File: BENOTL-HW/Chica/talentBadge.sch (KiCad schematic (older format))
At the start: 56 parts, among them P1 USB_A, P2 OLED, P3 Batt, P4 PS, Q1 MMBT3904, Q2 MMBT3904, Q3 IR phototransistor, SW1 B1, SW2 B2, SW3 RST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

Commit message: Agregado KeyStone_2479
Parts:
- P3: footprint Pin_Headers:Pin_Header_Straight_1x02_Pitch2.54mm -> talentBadge:Keystone_2479_3xAAA
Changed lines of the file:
@@
 LIBS:contrib
 LIBS:valves
-LIBS:pdxlbs
+LIBS:ESP8266
 LIBS:pspice
 LIBS:Video
-LIBS:Valve
 LIBS:Triac_Thyristor
-LIBS:Transistor_IGBT
-LIBS:Transistor_FET
-LIBS:Transistor_BJT
-LIBS:Transistor_Array
-LIBS:Transformer
-LIBS:Timer_RTC
-LIBS:Timer_PLL
-LIBS:Timer
-LIBS:Switch
-LIBS:Sensor_Voltage
-LIBS:Sensor_Touch
-LIBS:Sensor_Temperature
-LIBS:Sensor_Proximity
-LIBS:Sensor_Pressure
-LIBS:Sensor_Optical
-LIBS:Sensor_Motion
-LIBS:Sensor_Magnetic
-LIBS:Sensor_Humidity
-LIBS:Sensor_Gas
-LIBS:Sensor_Current
-LIBS:Sensor_Audio
-LIBS:Sensor
-LIBS:Relay_SolidState
-LIBS:Relay
-LIBS:Regulator_Switching
-LIBS:Regulator_SwitchedCapacitor
-LIBS:Regulator_Linear
-LIBS:Regulator_Current
-LIBS:Regulator_Controller
-LIBS:Reference_Voltage
-LIBS:Reference_Current
-LIBS:RF_ZigBee
-LIBS:RF_WiFi
-LIBS:RF_Switch
-LIBS:RF_RFID
-LIBS:RF_Module
-LIBS:RF_Mixer
-LIBS:RF_GPS
-LIBS:RF_Bluetooth
-LIBS:RF_AM_FM
-LIBS:RF
-LIBS:Power_Supervisor
-LIBS:Power_Protection
 LIBS:Power_Management
-LIBS:Potentiometer_Digital
-LIBS:Oscillator
-LIBS:Motor
-LIBS:Memory_UniqueID
-LIBS:Memory_ROM
-LIBS:Memory_RAM
-LIBS:Memory_NVRAM
-LIBS:Memory_Flash
-LIBS:Memory_EPROM
-LIBS:Memory_EEPROM
-LIBS:Memory_Controller
 LIBS:Mechanical
-LIBS:MCU_Texas_MSP430
-LIBS:MCU_Texas
-LIBS:MCU_SiliconLabs
-LIBS:MCU_SiFive
-LIBS:MCU_ST_STM8
-LIBS:MCU_ST_STM32
-LIBS:MCU_Parallax
-LIBS:MCU_NXP_S08
-LIBS:MCU_NXP_MCore
-LIBS:MCU_NXP_MAC7100
-LIBS:MCU_NXP_LPC
-LIBS:MCU_NXP_Kinetis
-LIBS:MCU_NXP_HCS12
-LIBS:MCU_NXP_HC12
-LIBS:MCU_NXP_HC11
-LIBS:MCU_NXP_ColdFire
-LIBS:MCU_Module
-LIBS:MCU_Microchip_SAML
-LIBS:MCU_Microchip_SAME
-LIBS:MCU_Microchip_PIC32
-LIBS:MCU_Microchip_PIC24
-LIBS:MCU_Microchip_PIC18
-LIBS:MCU_Microchip_PIC16
-LIBS:MCU_Microchip_PIC12
-LIBS:MCU_Microchip_PIC10
-LIBS:MCU_Intel
-LIBS:MCU_Infineon
-LIBS:MCU_Cypress
-LIBS:MCU_Atmel_AVR
-LIBS:MCU_Atmel_ATTINY
-LIBS:MCU_Atmel_ATMEGA
-LIBS:MCU_Atmel_8051
-LIBS:MCU_AnalogDevices
-LIBS:Logic_TTL_IEEE
 LIBS:Logic_Programmable
-LIBS:Logic_LevelTranslator
-LIBS:Logic_CMOS_IEEE
-LIBS:Logic_CMOS_4000
-LIBS:Logic_74xx
-LIBS:Logic_74xgxx
-LIBS:LED
-LIBS:Jumper
-LIBS:Isolator_Analog
-LIBS:Isolator
-LIBS:Interface_USB
-LIBS:Interface_UART
-LIBS:Interface_Telecom
-LIBS:Interface_Optical
-LIBS:Interface_LineDriver
-LIBS:Interface_HID
-LIBS:Interface_Expansion
-LIBS:Interface_Ethernet
-LIBS:Interface_CurrentLoop
-LIBS:Interface_CAN_LIN
 LIBS:Interface
 LIBS:Graphic
-LIBS:GPU
-LIBS:Filter
-LIBS:FPGA_Xilinx_Virtex7
-LIBS:FPGA_Xilinx_Virtex6
-LIBS:FPGA_Xilinx_Virtex5
-LIBS:FPGA_Xilinx_Spartan6
-LIBS:FPGA_Xilinx_Kintex7
-LIBS:FPGA_Xilinx_Artix7
-LIBS:FPGA_Xilinx
-LIBS:FPGA_Actel
-LIBS:Driver_Relay
-LIBS:Driver_Motor
-LIBS:Driver_LED
-LIBS:Driver_FET
-LIBS:Driver_Display
-LIBS:Display_Graphic
-LIBS:Display_Character
-LIBS:Diode_Laser
-LIBS:Diode_Bridge
 LIBS:Diode
 LIBS:Device
-LIBS:DSP_Texas
-LIBS:DSP_Motorola
-LIBS:DSP_Microchip_DSPIC33
-LIBS:DSP_Freescale
-LIBS:Converter_DCDC
-LIBS:Converter_ACDC
-LIBS:Connector_Specialized
-LIBS:Connector_Generic_Shielded
-LIBS:Connector_Generic
-LIBS:Comparator
-LIBS:CPU_PowerPC
-LIBS:CPU_NXP_68000
-LIBS:CPU_NXP_6800
-LIBS:CPU
-LIBS:CPLD_Xilinx
-LIBS:CPLD_Altera
 LIBS:Battery_Management
 LIBS:Audio
-LIBS:Analog_Switch
-LIBS:Analog_DAC
-LIBS:Analog_ADC
-LIBS:Analog
-LIBS:Amplifier_Video
-LIBS:Amplifier_Operational
-LIBS:Amplifier_Instrumentation
-LIBS:Amplifier_Difference
-LIBS:Amplifier_Current
-LIBS:Amplifier_Buffer
-LIBS:Amplifier_Audio
 LIBS:talentBadge-cache
 EELAYER 25 0
@@
 B2
 $Comp
-L +3.3V #PWR014
+L +3.3V #PWR011
 U 1 1 5A8ACE92
 P 8750 4150
-F 0 "#PWR014" H 8750 4000 50  0001 C CNN
+F 0 "#PWR011" H 8750 4000 50  0001 C CNN
 F 1 "+3.3V" H 8750 4290 50  0000 C CNN
 F 2 "" H 8750 4150 50  0000 C CNN
@@
 $EndComp
 $Comp
-L GND #PWR015
+L GND #PWR012
 U 1 1 5A8B6B0C
 P 8600 4600
-F 0 "#PWR015" H 8600 4350 50  0001 C CNN
+F 0 "#PWR012" H 8600 4350 50  0001 C CNN
 F 1 "GND" H 8450 4550 50  0000 C CNN
 F 2 "" H 8600 4600 50  0000 C CNN
@@
 $EndComp
 $Comp
-L GND #PWR016
+L GND #PWR013
 U 1 1 5A8BA4F2
 P 9050 6200
-F 0 "#PWR016" H 9050 5950 50  0001 C CNN
+F 0 "#PWR013" H 9050 5950 50  0001 C CNN
 F 1 "GND" H 9050 6050 50  0000 C CNN
 F 2 "" H 9050 6200 50  0000 C CNN
@@
 $EndComp
 $Comp
-L +3.3V #PWR017
+L +3.3V #PWR014
 U 1 1 5A8CF103
 P 3700 6000
-F 0 "#PWR017" H 3700 5850 50  0001 C CNN
+F 0 "#PWR014" H 3700 5850 50  0001 C CNN
 F 1 "+3.3V" H 3700 6140 50  0000 C CNN
 F 2 "" H 3700 6000 50  0000 C CNN
@@
 $EndComp
 $Comp
-L +3.3V #PWR018
+L +3.3V #PWR015
 U 1 1 5A8CF265
 P 4535 4300
-F 0 "#PWR018" H 4535 4150 50  0001 C CNN
+F 0 "#PWR015" H 4535 4150 50  0001 C CNN
 F 1 "+3.3V" H 4535 4440 50  0000 C CNN
 F 2 "" H 4535 4300 50  0000 C CNN
@@
 $EndComp
 $Comp
-L GND #PWR019
+L GND #PWR016
 U 1 1 5A8CFC33
 P 4650 4900
-F 0 "#PWR019" H 4650 4650 50  0001 C CNN
+F 0 "#PWR016" H 4650 4650 50  0001 C CNN
 F 1 "GND" H 4650 4750 50  0000 C CNN
 F 2 "" H 4650 4900 50  0000 C CNN
@@
 F 0 "P3" H 650 6500 50  0000 C CNN
 F 1 "Batt" V 750 6350 50  0000 C CNN
-F 2 "Pin_Headers:Pin_Header_Straight_1x02_Pitch2.54mm" H 650 6350 50  0001 C CNN
+F 2 "talentBadge:Keystone_2479_3xAAA" H 650 6350 50  0001 C CNN
 F 3 "" H 650 6350 50  0000 C CNN
 	1    650  6350
@@
 IRL
 $Comp
-L GND #PWR020
+L GND #PWR017
 U 1 1 5A914774
 P 6200 5150
-F 0 "#PWR020" H 6200 4900 50  0001 C CNN
+F 0 "#PWR017" H 6200 4900 50  0001 C CNN
 F 1 "GND" H 6200 5000 50  0000 C CNN
 F 2 "" H 6200 5150 50  0000 C CNN
@@
 $EndComp
 $Comp
-L +3.3V #PWR021
+L +3.3V #PWR018
 U 1 1 5A916FB2
 P 6200 3850
-F 0 "#PWR021" H 6200 3700 50  0001 C CNN
+F 0 "#PWR018" H 6200 3700 50  0001 C CNN
 F 1 "+3.3V" H 6200 3990 50  0000 C CNN
 F 2 "" H 6200 3850 50  0000 C CNN
@@
 $EndComp
 $Comp
-L +3.3V #PWR022
+L +3.3V #PWR019
 U 1 1 5A8CED38
 P 7775 1585
-F 0 "#PWR022" H 7775 1435 50  0001 C CNN
+F 0 "#PWR019" H 7775 1435 50  0001 C CNN
 F 1 "+3.3V" H 7775 1725 50  0000 C CNN
 F 2 "" H 7775 1585 50  0000 C CNN
@@
 NoConn ~ 10550 4800
 $Comp
-L GND #PWR023
+L GND #PWR020
 U 1 1 5A9146B5
 P 5700 5150
-F 0 "#PWR023" H 5700 4900 50  0001 C CNN
+F 0 "#PWR020" H 5700 4900 50  0001 C CNN
 F 1 "GND" H 5700 5000 50  0000 C CNN
 F 2 "" H 5700 5150 50  0000 C CNN
@@
 Connection ~ 8030 1475
 $Comp
-L +3.3V #PWR024
+L +3.3V #PWR021
 U 1 1 5AA16781
 P 8025 1415
-F 0 "#PWR024" H 8025 1265 50  0001 C CNN
+F 0 "#PWR021" H 8025 1265 50  0001 C CNN
 F 1 "+3.3V" H 8025 1555 50  0000 C CNN
 F 2 "" H 8025 1415 50  0000 C CNN
@@
 $EndComp
 $Comp
-L GND #PWR025
+L GND #PWR022
 U 1 1 5AA16E5F
 P 10830 2575
-F 0 "#PWR025" H 10830 2325 50  0001 C CNN
+F 0 "#PWR022" H 10830 2325 50  0001 C CNN
 F 1 "GND" H 10830 2425 50  0000 C CNN
 F 2 "" H 10830 2575 50  0000 C CNN
@@
 	9315 2940 9315 3060
 $Comp
-L GND #PWR026
+L GND #PWR023
 U 1 1 5AA1CD61
 P 9315 3060
-F 0 "#PWR026" H 9315 2810 50  0001 C CNN
+F 0 "#PWR023" H 9315 2810 50  0001 C CNN
 F 1 "GND" H 9315 2910 50  0000 C CNN
 F 2 "" H 9315 3060 50  0000 C CNN

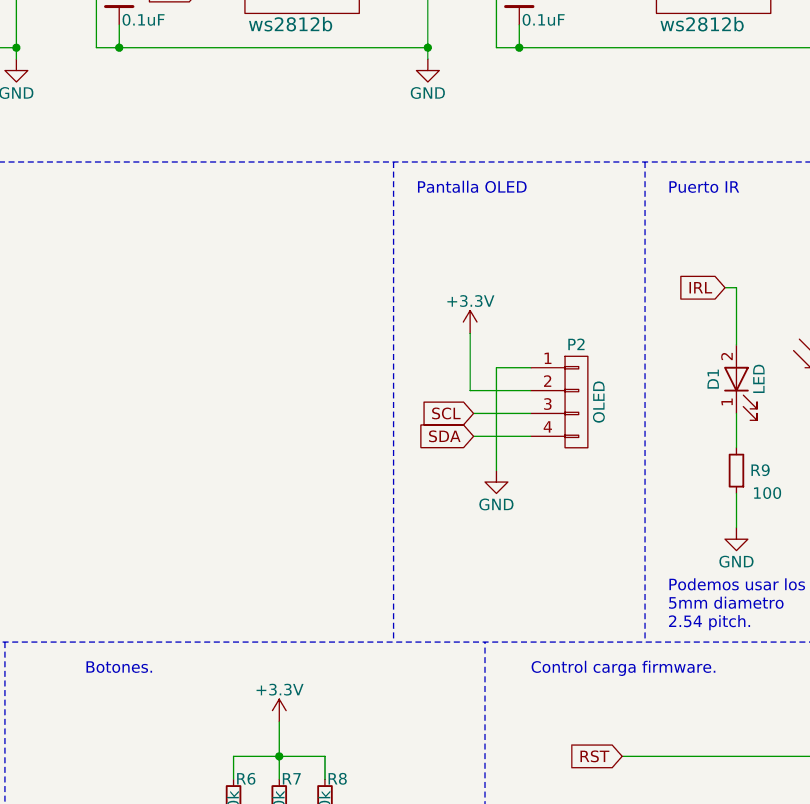
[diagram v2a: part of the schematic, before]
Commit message: Chica - I2C pullupt
Se agregan pullups a linea i2c para display.
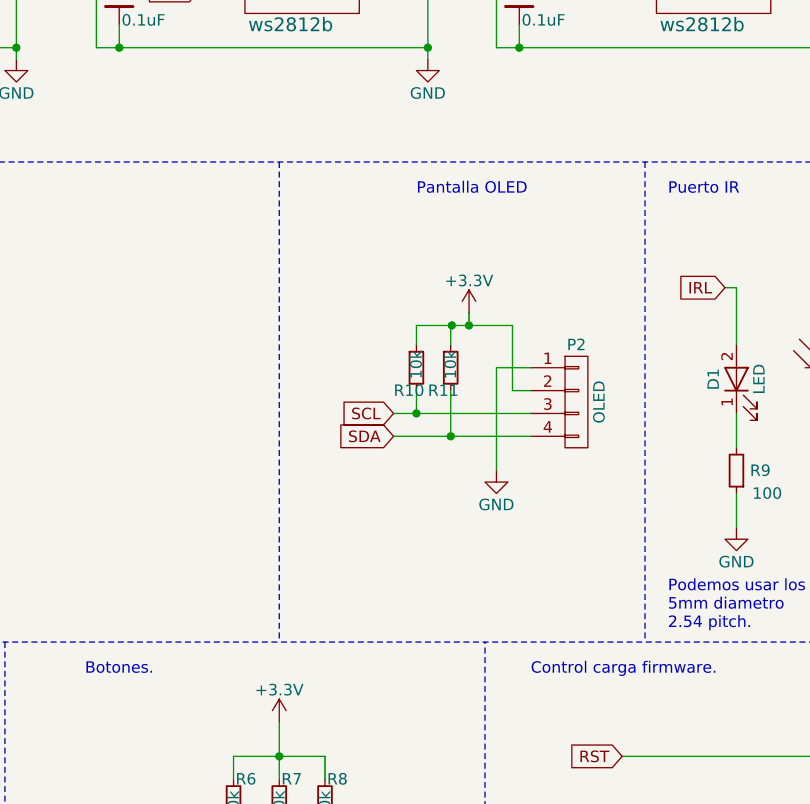
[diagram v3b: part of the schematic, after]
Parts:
- added R10, R11: 10k, Resistors_SMD:R_0805_HandSoldering, symbol R_Small
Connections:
- net +3V3: now also R10.1, R11.1
- net SCL: now also R10.2
- net SDA: now also R11.2
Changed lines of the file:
@@
 L +3.3V #PWR015
 U 1 1 5A8CF265
-P 4535 4300
-F 0 "#PWR015" H 4535 4150 50  0001 C CNN
-F 1 "+3.3V" H 4535 4440 50  0000 C CNN
-F 2 "" H 4535 4300 50  0000 C CNN
-F 3 "" H 4535 4300 50  0000 C CNN
-	1    4535 4300
+P 4530 4210
+F 0 "#PWR015" H 4530 4060 50  0001 C CNN
+F 1 "+3.3V" H 4530 4350 50  0000 C CNN
+F 2 "" H 4530 4210 50  0000 C CNN
+F 3 "" H 4530 4210 50  0000 C CNN
+	1    4530 4210
 	1    0    0    -1
 $EndComp
@@
 	1    0    0    -1
 $EndComp
-Text GLabel 4550 4750 0    50   Input ~ 0
+Text GLabel 4200 4750 0    50   Input ~ 0
 SDA
-Text GLabel 4550 4650 0    50   Input ~ 0
+Text GLabel 4200 4650 0    50   Input ~ 0
 SCL
 Text GLabel 8090 2140 0    50   Output ~ 0
@@
 	1    0    0    -1
 $EndComp
+$Comp
+L +3.3V #PWR021
+U 1 1 5AA16781
+P 8025 1415
+F 0 "#PWR021" H 8025 1265 50  0001 C CNN
+F 1 "+3.3V" H 8025 1555 50  0000 C CNN
+F 2 "" H 8025 1415 50  0000 C CNN
+F 3 "" H 8025 1415 50  0000 C CNN
+	1    8025 1415
+	1    0    0    -1
+$EndComp
+$Comp
+L GND #PWR022
+U 1 1 5AA16E5F
+P 10830 2575
+F 0 "#PWR022" H 10830 2325 50  0001 C CNN
+F 1 "GND" H 10830 2425 50  0000 C CNN
+F 2 "" H 10830 2575 50  0000 C CNN
+F 3 "" H 10830 2575 50  0000 C CNN
+	1    10830 2575
+	1    0    0    -1
+$EndComp
+NoConn ~ 10485 1940
+$Comp
+L GND #PWR023
+U 1 1 5AA1CD61
+P 9315 3060
+F 0 "#PWR023" H 9315 2810 50  0001 C CNN
+F 1 "GND" H 9315 2910 50  0000 C CNN
+F 2 "" H 9315 3060 50  0000 C CNN
+F 3 "" H 9315 3060 50  0000 C CNN
+	1    9315 3060
+	1    0    0    -1
+$EndComp
+$Comp
+L R_Small R10
+U 1 1 5AA6BBDB
+P 4300 4450
+F 0 "R10" H 4200 4350 50  0000 L CNN
+F 1 "10k" V 4300 4400 50  0000 L CNN
+F 2 "Resistors_SMD:R_0805_HandSoldering" H 4300 4450 50  0001 C CNN
+F 3 "https://www.mouser.com/ds/2/447/Yageo_08112016_RC0805-1211991.pdf" H 4300 4450 50  0001 C CNN
+F 4 "RC0805FR-0710KL" H 4300 4450 60  0001 C CNN "PartNo"
+	1    4300 4450
+	1    0    0    -1
+$EndComp
+$Comp
+L R_Small R11
+U 1 1 5AA6BCEE
+P 4450 4450
+F 0 "R11" H 4350 4350 50  0000 L CNN
+F 1 "10k" V 4450 4400 50  0000 L CNN
+F 2 "Resistors_SMD:R_0805_HandSoldering" H 4450 4450 50  0001 C CNN
+F 3 "https://www.mouser.com/ds/2/447/Yageo_08112016_RC0805-1211991.pdf" H 4450 4450 50  0001 C CNN
+F 4 "RC0805FR-0710KL" H 4450 4450 60  0001 C CNN "PartNo"
+	1    4450 4450
+	1    0    0    -1
+$EndComp
 Wire Wire Line
 	3000 6550 2900 6550
@@
 Connection ~ 3900 6850
 Wire Wire Line
-	4535 4300 4535 4550
-Wire Wire Line
 	4650 4450 4650 4900
 Wire Wire Line
-	4550 4650 4800 4650
-Wire Wire Line
-	4800 4750 4550 4750
+	4200 4650 4800 4650
+Wire Wire Line
+	4200 4750 4800 4750
 Wire Wire Line
 	8100 2440 8100 2640
@@
 	6900 5650 6900 5600
 Wire Notes Line
-	4200 3550 4200 5650
+	3700 3550 3700 5650
 Wire Wire Line
 	8100 4800 9350 4800
@@
 	4650 4450 4800 4450
 Wire Wire Line
-	4535 4550 4800 4550
-Wire Wire Line
 	8315 1740 8075 1740
 Wire Wire Line
@@
 	8030 1415 8025 1415
 Connection ~ 8030 1475
-$Comp
-L +3.3V #PWR021
-U 1 1 5AA16781
-P 8025 1415
-F 0 "#PWR021" H 8025 1265 50  0001 C CNN
-F 1 "+3.3V" H 8025 1555 50  0000 C CNN
-F 2 "" H 8025 1415 50  0000 C CNN
-F 3 "" H 8025 1415 50  0000 C CNN
-	1    8025 1415
-	1    0    0    -1
-$EndComp
-$Comp
-L GND #PWR022
-U 1 1 5AA16E5F
-P 10830 2575
-F 0 "#PWR022" H 10830 2325 50  0001 C CNN
-F 1 "GND" H 10830 2425 50  0000 C CNN
-F 2 "" H 10830 2575 50  0000 C CNN
-F 3 "" H 10830 2575 50  0000 C CNN
-	1    10830 2575
-	1    0    0    -1
-$EndComp
 Wire Wire Line
 	10830 1740 10830 2575
 Connection ~ 10830 2240
-NoConn ~ 10485 1940
 Wire Wire Line
 	8315 2440 8000 2440
@@
 Wire Wire Line
 	9315 2940 9315 3060
-$Comp
-L GND #PWR023
-U 1 1 5AA1CD61
-P 9315 3060
-F 0 "#PWR023" H 9315 2810 50  0001 C CNN
-F 1 "GND" H 9315 2910 50  0000 C CNN
-F 2 "" H 9315 3060 50  0000 C CNN
-F 3 "" H 9315 3060 50  0000 C CNN
-	1    9315 3060
-	1    0    0    -1
-$EndComp
+Wire Wire Line
+	4300 4350 4300 4265
+Wire Wire Line
+	4300 4265 4720 4265
+Wire Wire Line
+	4530 4265 4530 4210
+Wire Wire Line
+	4450 4350 4450 4265
+Wire Wire Line
+	4450 4265 4455 4265
+Connection ~ 4455 4265
+Wire Wire Line
+	4720 4265 4720 4550
+Wire Wire Line
+	4720 4550 4800 4550
+Connection ~ 4530 4265
+Wire Wire Line
+	4450 4550 4450 4750
+Connection ~ 4450 4750
+Wire Wire Line
+	4300 4550 4300 4650
+Connection ~ 4300 4650
 $EndSCHEMATC
